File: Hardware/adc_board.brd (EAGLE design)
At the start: 30.5 x 44.5 mm, 21 parts, among them U1 ADS1015, U2 PCA9306

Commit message: Board ready for review
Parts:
- moved JP1 80.7 mm to (6.35, 49.5)
- moved C1 77.8 mm to (14.0, 30.5)
- moved SJ3 67.6 mm to (11.4, 24.1)
- moved R3 65.9 mm to (10.2, 15.2), turned to 180 degrees
- moved SJ4 64.9 mm to (14.0, 24.1)
- moved R1 64.4 mm to (15.2, 20.3)
- moved U1 62.1 mm to (14.0, 33.0), turned to 90 degrees
- moved R4 61.4 mm to (12.7, 10.8), turned to 180 degrees
- moved C2 60.9 mm to (7.62, 16.5), turned to 180 degrees
- moved SJ1 60.8 mm to (6.35, 24.1)
- moved R2 60.7 mm to (11.4, 19.1), turned to 180 degrees
- moved R5 58.5 mm to (12.7, 9.53), turned to 180 degrees
- moved SJ2 57.8 mm to (8.89, 24.1)
- moved C3 55.7 mm to (10.2, 11.4), turned to 270 degrees
- moved U2 53.0 mm to (12.7, 15.2)
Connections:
- removed net LV_SCL: R4.1, U2.2
- removed net LV_SDA: R5.1, U2.3
- removed net SCL: SJ4.2
- removed net SDA: SJ3.2
- removed net VDD: C1.1, C2.1, R1.2, R2.2, R3.2, SJ2.2, U1.8
- net ADDR: now also U1.1; no longer U1.2
- net GP19_I2C_1_SCL: now also R4.1, U2.2
- net GP20_I2C_1_SDA: now also R5.1, U2.3
- net HV_SCL: now also SJ4.2
- net HV_SDA: now also SJ3.2
- net VSYS: now also C1.1, C2.1, R1.2, R2.2, R3.2, SJ2.2, U1.8
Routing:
- net VSYS: track 4.48 -> 46.8 mm, vias 1 -> 4
- net GND: track 0.00 -> 30.3 mm, vias 2 -> 3
- net HV_SCL: track 0.00 -> 28.8 mm, vias 0 -> 3
- net ADDR: track 0.00 -> 27.5 mm
- net GP19_I2C_1_SCL: track 7.37 -> 33.9 mm, vias 1 -> 2
- net GP20_I2C_1_SDA: track 2.97 -> 29.2 mm
- net HV_SDA: track 0.00 -> 23.0 mm, vias 0 -> 2
- net 1.8V: track 4.25 -> 26.9 mm
- net N$5: track 0.00 -> 21.4 mm
- net N$2: track 0.00 -> 21.4 mm
- net N$4: track 0.00 -> 17.0 mm
- net N$3: track 0.00 -> 16.8 mm
- net N$1: track 0.00 -> 4.11 mm
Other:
- board size 30.5 x 44.5 mm -> 30.5 x 50.8 mm

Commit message: Add version info
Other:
- board text added: "v01"
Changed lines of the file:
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@@
 <dimension x1="29.28210625" y1="41.83789375" x2="27.86789375" y2="43.25210625" x3="34.29" y3="48.26" textsize="1.778" layer="51" dtype="diameter"/>
 <text x="29.21" y="6.35" size="1.016" layer="22" font="vector" ratio="15" rot="MR90" align="center">4xM2.0</text>
+<text x="1.27" y="3.81" size="1.778" layer="1" font="vector" ratio="15">v01</text>
 </plain>
 <attributes>

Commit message: Updated to new edison.lbr
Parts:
- moved C2 1.27 mm to (7.62, 17.8), turned to 90 degrees
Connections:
- net N$2 renamed A1-/AIN3
- net N$3 renamed A1+/AIN2
- net N$4 renamed A0-/AIN1
- net N$5 renamed A0+/AIN0
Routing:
- net VSYS: track 46.8 -> 48.9 mm
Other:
- board text added: "12-Bit ADC"
- board text added: "A0+/AIN0"
- board text added: "A0-/AIN1"
- board text added: "A0-/AIN3"
- board text added: "A1+/AIN2"
- board text added: "GND"
- board text removed: "Example Name of Board"
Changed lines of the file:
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@@
 <text x="-2.54" y="41.91" size="1.778" layer="51" rot="R270">LED's and selector switches go here</text>
 <text x="31.115" y="39.37" size="1.778" layer="51" rot="R270">Nothing goes here...  I mean it.</text>
-<text x="29.337" y="29.21" size="1.27" layer="22" font="vector" ratio="15" rot="MR90" align="center">Example Name of Board</text>
+<text x="29.337" y="29.21" size="1.27" layer="22" font="vector" ratio="15" rot="MR90" align="center">12-Bit ADC</text>
 <wire x1="1.778" y1="50.8" x2="28.702" y2="50.8" width="0.1524" layer="20"/>
 <wire x1="30.48" y1="44.704" x2="30.48" y2="50.8" width="0.254" layer="51"/>
@@
 <text x="29.21" y="6.35" size="1.016" layer="22" font="vector" ratio="15" rot="MR90" align="center">4xM2.0</text>
 <text x="1.27" y="3.81" size="1.778" layer="1" font="vector" ratio="15">v01</text>
+<text x="8.89" y="48.26" size="1.778" layer="22" font="vector" ratio="15" rot="MR90" align="center-right">GND</text>
+<text x="13.97" y="48.26" size="1.778" layer="22" font="vector" ratio="15" rot="MR90" align="center-right">GND</text>
+<text x="19.05" y="48.26" size="1.778" layer="22" font="vector" ratio="15" rot="MR90" align="center-right">GND</text>
+<text x="24.13" y="48.26" size="1.778" layer="22" font="vector" ratio="15" rot="MR90" align="center-right">GND</text>
+<text x="6.35" y="48.26" size="1.016" layer="22" font="vector" ratio="15" rot="MR90" align="center-right">A0-/AIN3</text>
+<text x="11.43" y="48.26" size="1.016" layer="22" font="vector" ratio="15" rot="MR90" align="center-right">A1+/AIN2</text>
+<text x="16.51" y="48.26" size="1.016" layer="22" font="vector" ratio="15" rot="MR90" align="center-right">A0-/AIN1</text>
+<text x="21.59" y="48.26" size="1.016" layer="22" font="vector" ratio="15" rot="MR90" align="center-right">A0+/AIN0</text>
 </plain>
 <attributes>
@@
 <element name="SJ3" library="SparkFun-Passives" package="PAD-JUMPER-2-NO_YES_SILK" value="JUMPER-PAD-2-NOYES_SILK" x="11.43" y="24.13"/>
 <element name="SJ4" library="SparkFun-Passives" package="PAD-JUMPER-2-NO_YES_SILK" value="JUMPER-PAD-2-NOYES_SILK" x="13.97" y="24.13"/>
-<element name="C2" library="SparkFun-Capacitors" package="0603-CAP" value="0.1uF" x="7.62" y="16.51" rot="R180">
-<attribute name="PROD_ID" value="CAP-00810" x="35.56" y="5.08" size="1.778" layer="27" font="vector" ratio="15" rot="R180" display="off"/>
+<element name="C2" library="SparkFun-Capacitors" package="0603-CAP" value="0.1uF" x="7.62" y="17.78" rot="R90">
+<attribute name="PROD_ID" value="CAP-00810" x="-3.81" y="-10.16" size="1.778" layer="27" font="vector" ratio="15" rot="R90" display="off"/>
 </element>
 <element name="C3" library="SparkFun-Capacitors" package="0603-CAP" value="0.1uF" x="10.16" y="11.43" rot="R270">
@@
 <contactref element="R3" pad="2"/>
 <contactref element="SJ2" pad="2"/>
-<wire x1="8.47" y1="16.51" x2="9.398" y2="16.51" width="0.254" layer="1"/>
-<wire x1="9.398" y1="16.51" x2="9.779" y2="16.51" width="0.254" layer="1"/>
-<wire x1="9.779" y1="16.51" x2="10.541" y2="17.272" width="0.254" layer="1"/>
+<wire x1="9.31" y1="16.041" x2="10.541" y2="17.272" width="0.254" layer="1"/>
 <wire x1="10.541" y1="17.272" x2="10.541" y2="19.011" width="0.254" layer="1"/>
 <wire x1="10.541" y1="19.011" x2="10.58" y2="19.05" width="0.254" layer="1"/>
-<wire x1="9.31" y1="15.24" x2="9.31" y2="16.422" width="0.254" layer="1"/>
-<wire x1="9.31" y1="16.422" x2="9.398" y2="16.51" width="0.254" layer="1"/>
 <wire x1="10.58" y1="19.05" x2="10.58" y2="21.17" width="0.254" layer="1"/>
 <wire x1="10.58" y1="21.17" x2="9.34" y2="22.41" width="0.254" layer="1"/>
@@
 <wire x1="16.51" y1="22.352" x2="16.09" y2="21.932" width="0.254" layer="1"/>
 <wire x1="16.536" y1="22.58" x2="16.51" y2="22.606" width="0.254" layer="1"/>
+<wire x1="7.62" y1="16.93" x2="7.62" y2="15.494" width="0.254" layer="1"/>
+<wire x1="7.62" y1="15.494" x2="7.874" y2="15.24" width="0.254" layer="1"/>
+<wire x1="7.874" y1="15.24" x2="9.31" y2="15.24" width="0.254" layer="1"/>
+<wire x1="9.31" y1="15.24" x2="9.31" y2="16.041" width="0.254" layer="1"/>
 </signal>
 <signal name="3.3V">
@@
 <wire x1="13.52" y1="26.601" x2="13.589" y2="26.67" width="0.254" layer="1"/>
 </signal>
-<signal name="N$2">
+<signal name="A1-/AIN3">
 <contactref element="JP1" pad="1"/>
 <contactref element="U1" pad="7"/>
@@
 <wire x1="6.35" y1="33.909" x2="6.35" y2="49.53" width="0.254" layer="1"/>
 </signal>
-<signal name="N$3">
+<signal name="A1+/AIN2">
 <contactref element="U1" pad="6"/>
 <contactref element="JP1" pad="3"/>
@@
 <wire x1="11.43" y1="35.56" x2="11.43" y2="49.53" width="0.254" layer="1"/>
 </signal>
-<signal name="N$4">
+<signal name="A0-/AIN1">
 <contactref element="JP1" pad="5"/>
 <contactref element="U1" pad="5"/>
@@
 <wire x1="16.51" y1="35.687" x2="16.51" y2="49.53" width="0.254" layer="1"/>
 </signal>
-<signal name="N$5">
+<signal name="A0+/AIN0">
 <contactref element="U1" pad="4"/>
 <contactref element="JP1" pad="7"/>

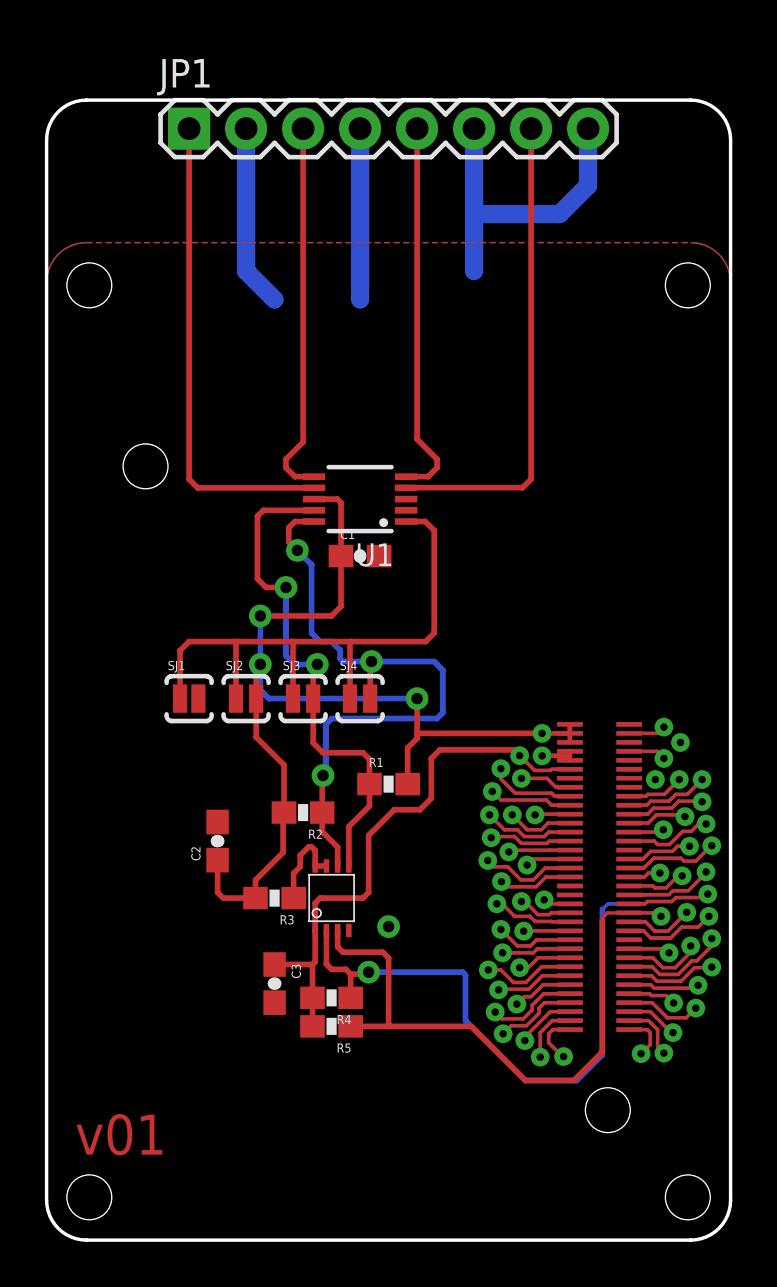
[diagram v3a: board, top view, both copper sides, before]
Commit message: Incorporate review feedback
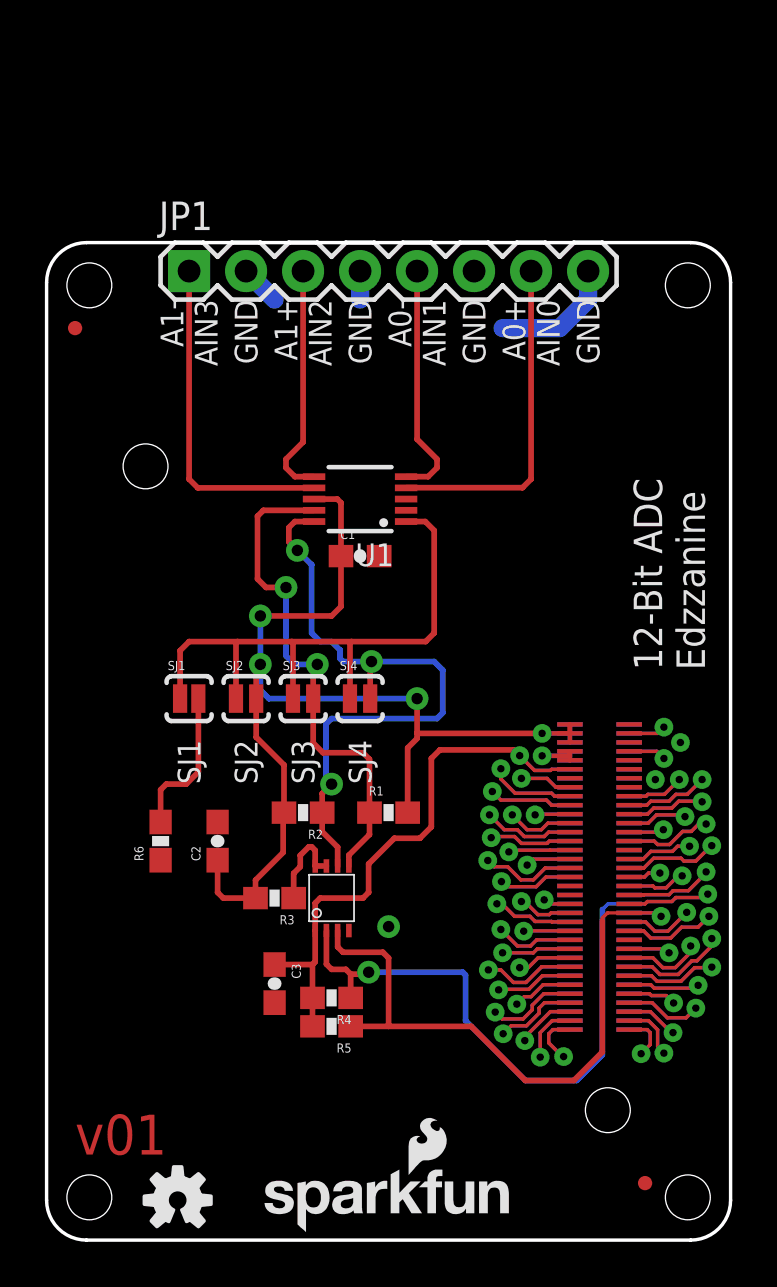
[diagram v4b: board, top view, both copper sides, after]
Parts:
- added FID1, FID2: FIDUCIALUFIDUCIAL, SparkFun-Aesthetics:MICRO-FIDUCIAL
- added LOGO1: SFE_LOGO_NAME_FLAME.1_INCH, SparkFun-Aesthetics:SFE_LOGO_NAME_FLAME_.1
- added LOGO4: OSHW-LOGOS, SparkFun-Aesthetics:OSHW-LOGO-S
- added R6: 2.2k, SparkFun-Resistors:0603-RES
- moved JP1 6.35 mm to (6.35, 43.2)
- moved R1 1.27 mm to (15.2, 19.1)
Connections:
- new net N$3: R6.2, SJ1.2
- net GND: now also R6.1; no longer SJ1.2
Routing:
- net GND: track 30.3 -> 8.67 mm
- net N$3: track 0.00 -> 6.72 mm
- net A1+/AIN2: track 16.8 -> 10.5 mm
- net A1-/AIN3: track 21.4 -> 15.0 mm
- net A0-/AIN1: track 17.0 -> 10.7 mm
- net A0+/AIN0: track 21.4 -> 15.0 mm
- net VSYS: track 48.9 -> 50.2 mm
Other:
- board size 30.5 x 50.8 mm -> 30.5 x 44.5 mm
- board text added: "12-Bit ADC Edzzanine"
- board text added: "A0+ AIN0"
- board text added: "A0- AIN1"
- board text added: "A1+ AIN2"
- board text added: "A1- AIN3"
- board text added: "M Hord"
- board text added: "SJ1"
- board text added: "SJ2"
- board text added: "SJ3"
- board text added: "SJ4"
- board text removed: "12-Bit ADC"
- board text removed: "A0+/AIN0"
- board text removed: "A0-/AIN1"
- board text removed: "A0-/AIN3"
- board text removed: "A1+/AIN2"
- board text removed: "Casey Kuhns"

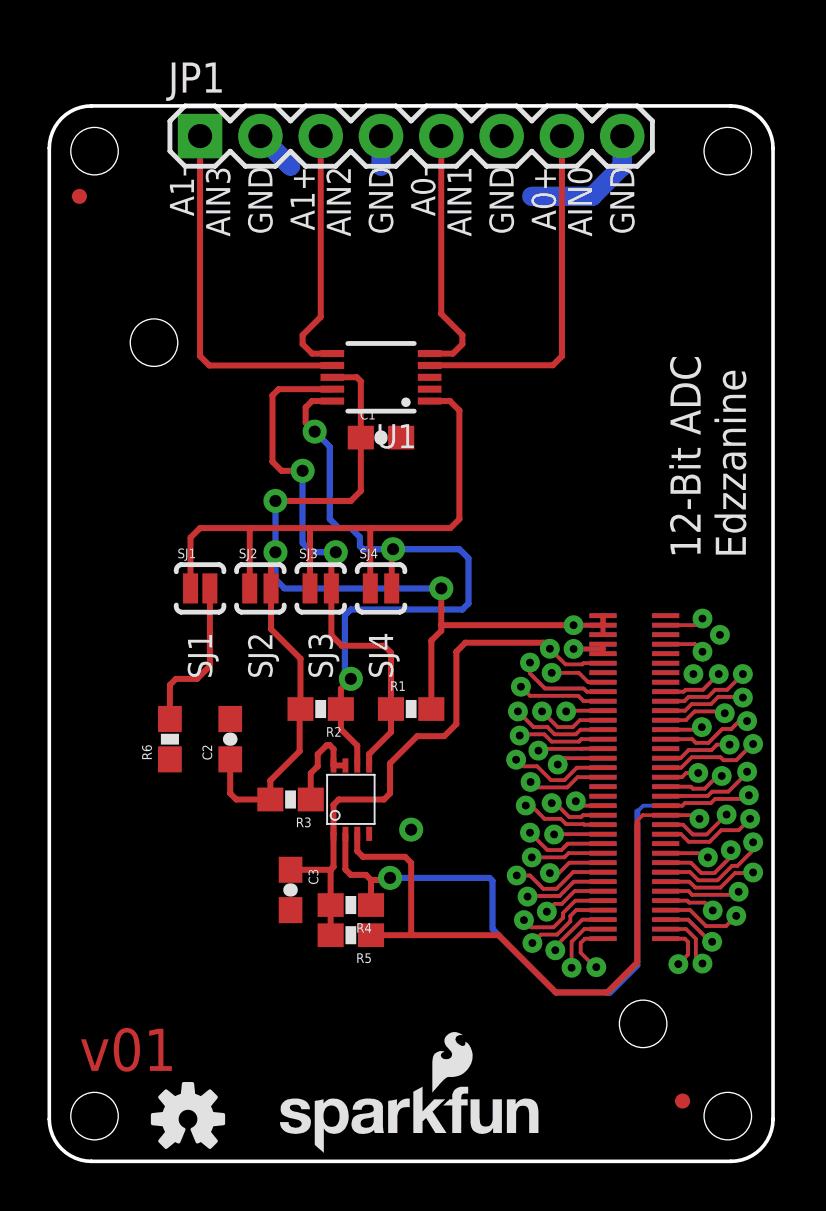
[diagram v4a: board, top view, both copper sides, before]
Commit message: Fix fids, remove weird name
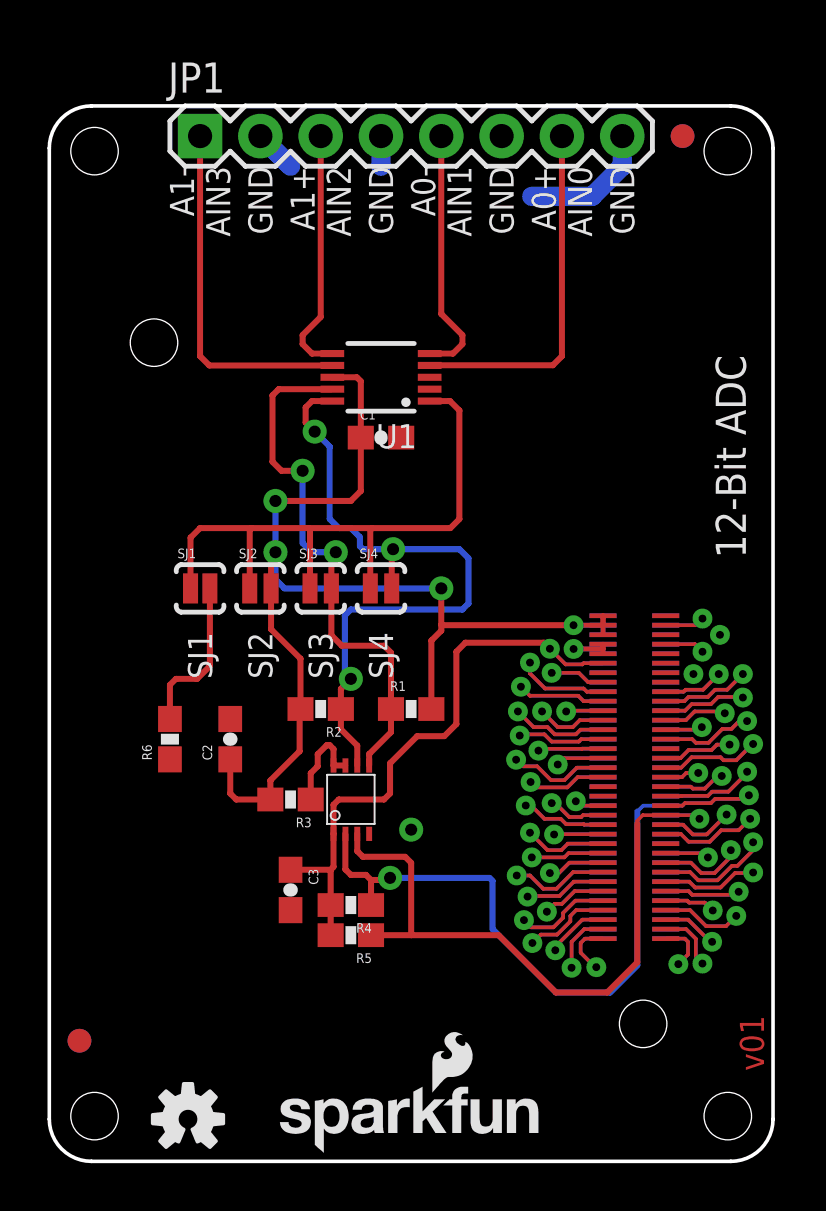
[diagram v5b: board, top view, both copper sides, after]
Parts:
- added FID3, FID4: FIDUCIAL1X2, SparkFun-Aesthetics:FIDUCIAL-1X2
- FID1, FID2: value FIDUCIALUFIDUCIAL -> FIDUCIAL1X2; device SparkFun-Aesthetics:MICRO-FIDUCIAL -> SparkFun-Aesthetics:FIDUCIAL-1X2
- moved FID1 25.5 mm to (1.27, 5.08)
- moved FID2 25.5 mm to (26.7, 43.2)
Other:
- board text added: "12-Bit ADC"
- board text removed: "12-Bit ADC Edzzanine"
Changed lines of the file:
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@@
 <text x="-2.54" y="41.91" size="1.778" layer="51" rot="R270">LED's and selector switches go here</text>
 <text x="31.115" y="39.37" size="1.778" layer="51" rot="R270">Nothing goes here...  I mean it.</text>
-<text x="26.797" y="25.4" size="1.27" layer="22" font="vector" ratio="15" rot="MR90">12-Bit ADC
-Edzzanine</text>
+<text x="28.067" y="25.4" size="1.27" layer="22" font="vector" ratio="15" rot="MR90">12-Bit ADC</text>
 <wire x1="1.778" y1="44.45" x2="28.702" y2="44.45" width="0.1524" layer="20"/>
 <wire x1="30.48" y1="44.704" x2="30.48" y2="50.8" width="0.254" layer="51"/>
@@
 <wire x1="28.702" y1="44.45" x2="30.48" y2="42.672" width="0.1524" layer="20" curve="-90"/>
 <text x="14.986" y="51.816" size="1.27" layer="51" ratio="15" align="center">Max Board Length</text>
-<dimension x1="28.575" y1="1.905" x2="1.905" y2="1.905" x3="15.24" y3="-2.54" textsize="1.27" textratio="15" layer="51" dtype="horizontal" unit="inch"/>
+<dimension x1="28.575" y1="1.905" x2="1.905" y2="1.905" x3="15.24" y3="-2.54" textsize="1.778" textratio="15" layer="51" dtype="horizontal" unit="inch"/>
 <dimension x1="30.48" y1="1.728" x2="0" y2="2.54" x3="15.24" y3="-5.08" textsize="1.27" textratio="15" layer="51" dtype="horizontal" unit="inch"/>
 <dimension x1="1.905" y1="42.545" x2="1.905" y2="1.905" x3="35.56" y3="22.225" textsize="1.27" textratio="15" layer="51" dtype="vertical" unit="inch"/>
@@
 <dimension x1="29.28210625" y1="41.83789375" x2="27.86789375" y2="43.25210625" x3="34.29" y3="48.26" textsize="1.778" layer="51" dtype="diameter"/>
 <text x="29.21" y="6.35" size="1.016" layer="22" font="vector" ratio="15" rot="MR90" align="center">4xM2.0</text>
-<text x="1.27" y="3.81" size="1.778" layer="1" font="vector" ratio="15">v01</text>
+<text x="30.099" y="3.81" size="1.016" layer="1" font="vector" ratio="15" rot="R90">v01</text>
 <text x="8.89" y="41.91" size="1.016" layer="22" font="vector" ratio="15" rot="MR90" align="center-right">GND</text>
 <text x="13.97" y="41.91" size="1.016" layer="22" font="vector" ratio="15" rot="MR90" align="center-right">GND</text>
@@
 AIN0</text>
 <text x="24.13" y="41.91" size="1.016" layer="21" font="vector" ratio="15" rot="R90" align="center-right">GND</text>
-<text x="29.337" y="25.4" size="1.27" layer="21" font="vector" ratio="15" rot="R90">12-Bit ADC
-Edzzanine</text>
+<text x="29.337" y="25.4" size="1.27" layer="21" font="vector" ratio="15" rot="R90">12-Bit ADC</text>
 <text x="6.35" y="20.32" size="1.016" layer="21" font="vector" ratio="15" rot="R90" align="center-left">SJ1</text>
 <text x="8.89" y="20.32" size="1.016" layer="21" font="vector" ratio="15" rot="R90" align="center-left">SJ2</text>
@@
 <attribute name="PROD_ID" value="RES-08272" x="5.08" y="17.78" size="1.778" layer="27" font="vector" ratio="15" rot="R90" display="off"/>
 </element>
-<element name="FID1" library="SparkFun-Aesthetics" package="MICRO-FIDUCIAL" value="FIDUCIALUFIDUCIAL" x="26.67" y="2.54"/>
-<element name="FID2" library="SparkFun-Aesthetics" package="MICRO-FIDUCIAL" value="FIDUCIALUFIDUCIAL" x="1.27" y="40.64"/>
+<element name="FID1" library="SparkFun-Aesthetics" package="FIDUCIAL-1X2" value="FIDUCIAL1X2" x="1.27" y="5.08"/>
+<element name="FID2" library="SparkFun-Aesthetics" package="FIDUCIAL-1X2" value="FIDUCIAL1X2" x="26.67" y="43.18"/>
+<element name="FID3" library="SparkFun-Aesthetics" package="FIDUCIAL-1X2" value="FIDUCIAL1X2" x="26.67" y="43.18" rot="MR0"/>
+<element name="FID4" library="SparkFun-Aesthetics" package="FIDUCIAL-1X2" value="FIDUCIAL1X2" x="1.27" y="5.08" rot="MR0"/>
 </elements>
 <signals>
